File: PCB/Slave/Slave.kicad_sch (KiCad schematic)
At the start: 54 parts, among them J1 USB_C_Receptacle_USB2.0_16P, J2 Conn_01x05_Pin, J3 Conn_01x07_Socket, J4 Conn_01x04_Socket, J5 Conn_01x07_Socket, Q2 PNP, SW1 PTS810_SJM_250_SMTR_LFS, SW2 PTS810_SJM_250_SMTR_LFS, U1 ESP32-S3-MINI-1, U2 TCA9406DC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

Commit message: PCB-Update
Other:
- moved on the sheet: C1, C10, C12, C20, C9, J2, R11, U1

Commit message: Small changes to the pcb(Master and Slave))
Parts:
- C1: value u1F -> 100nF
- C19, C3, C4, C5, C7, C9: value 0u1F -> 100nF
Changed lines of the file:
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@@
 		(dnp no)
 		(property "Reference" "C5"
-			(at 86.9935 152.2437 90)
+			(at 92.964 153.416 90)
 			(effects
 				(font
@@
 			)
 		)
-		(property "Value" "0u1F"
-			(at 83.1835 152.2437 90)
+		(property "Value" "100nF"
+			(at 91.186 156.718 90)
 			(effects
 				(font
 					(size 1.27 1.27)
 				)
-				(hide yes)
 			)
 		)
@@
 			)
 		)
-		(property "Value" "u1F"
-			(at 325.12 45.212 0)
+		(property "Value" "100nF"
+			(at 323.088 45.212 0)
 			(effects
 				(font
@@
 			)
 		)
-		(property "Value" "0u1F"
+		(property "Value" "100nF"
 			(at 217.297 200.406 0)
 			(effects
@@
 			)
 		)
-		(property "Value" "0u1F"
+		(property "Value" "100nF"
 			(at 42.164 128.016 0)
 			(effects
@@
 			)
 		)
-		(property "Value" "0u1F"
+		(property "Value" "100nF"
 			(at 59.182 160.782 0)
 			(effects
@@
 			)
 		)
-		(property "Value" "0u1F"
+		(property "Value" "100nF"
 			(at 84.074 128.016 0)
 			(effects
@@
 		)
 		(property "Value" "GND"
-			(at 366.776 179.578 0)
+			(at 367.792 182.372 0)
 			(effects
 				(font
@@
 			)
 		)
-		(property "Value" "0u1F"
+		(property "Value" "100nF"
 			(at 364.744 178.816 0)
 			(effects

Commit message: Added CAP
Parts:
- added C21, C23: 100nF, Capacitor_SMD:C_0603_1608Metric_Pad1.08x0.95mm_HandSolder, symbol Device:C
- added C22: 1uF, Capacitor_SMD:C_0603_1608Metric_Pad1.08x0.95mm_HandSolder, symbol Device:C
- added C24: u1F, Capacitor_SMD:C_0603_1608Metric_Pad1.08x0.95mm_HandSolder, symbol Device:C
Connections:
- net ESP_3V3: now also C11.1, Q2.3 (E), U5.1 (VSUP), U5.16 (DVDD), C21.1, C22.1, C24.1
- net GND: now also C21.2, C22.2, C23.1, C24.2
- net VCC_5V: now also C23.2
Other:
- moved on the sheet: C1, C10, C11, C12, C13, C14, C15, C16, C17, C18, C19, C20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

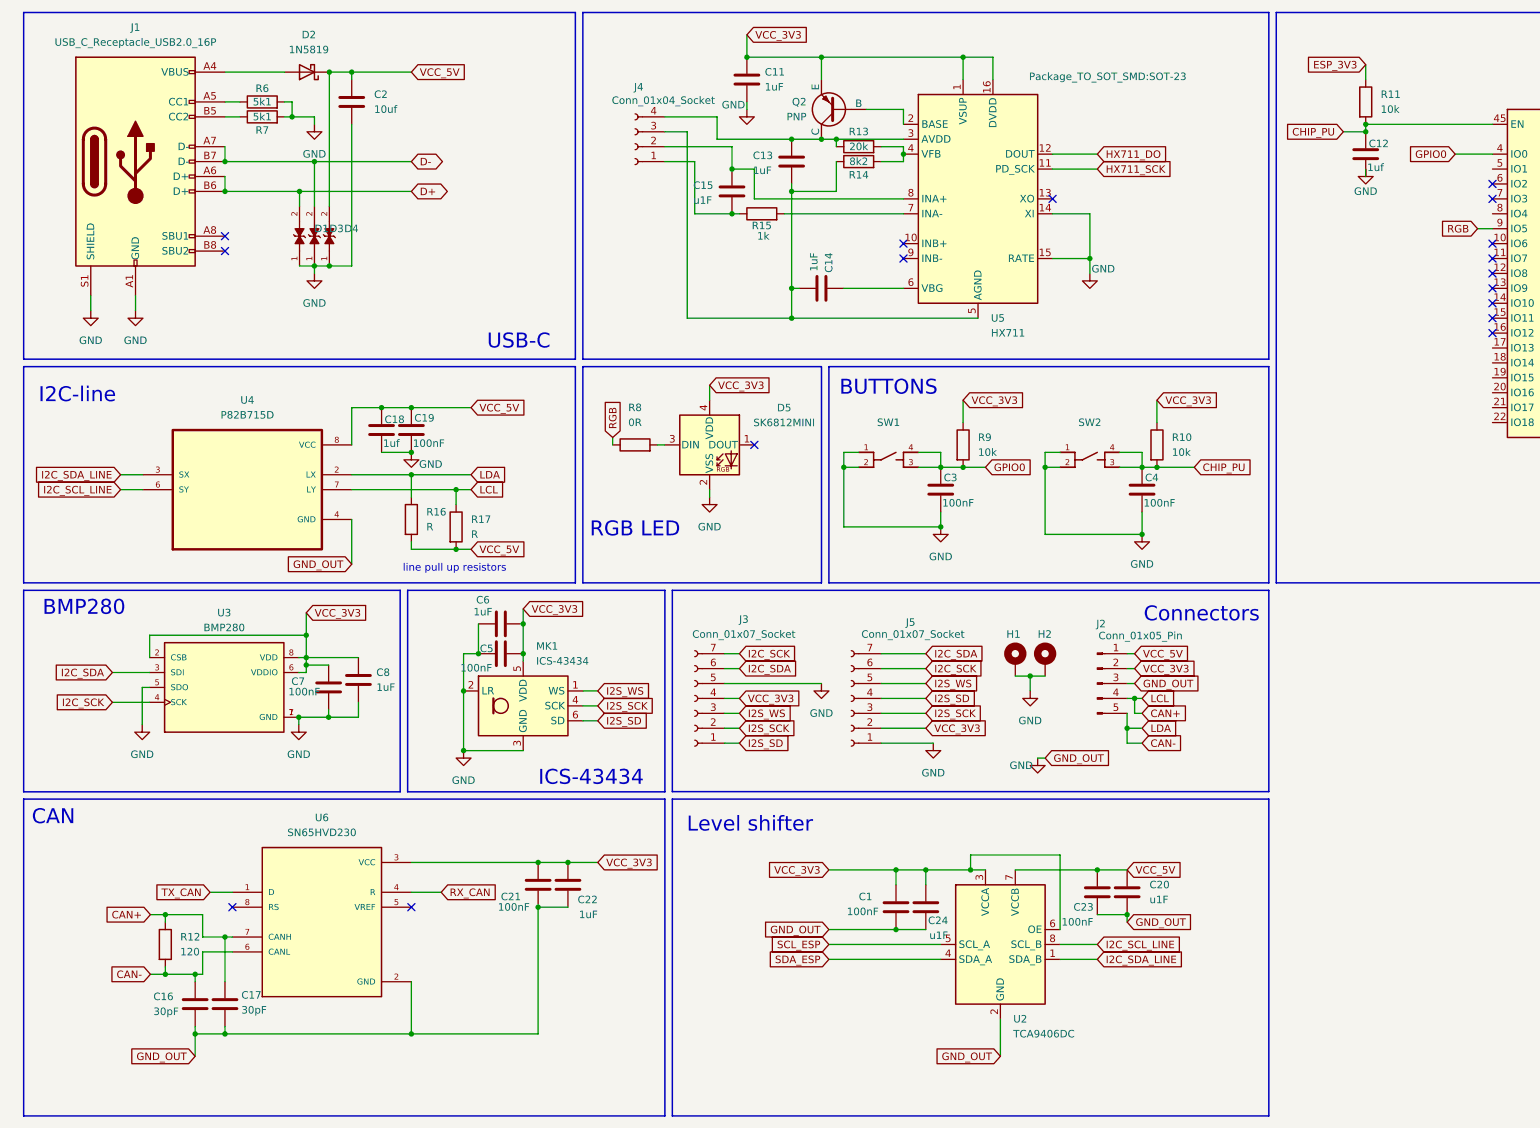
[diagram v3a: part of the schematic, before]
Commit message: Changed bmp for bme
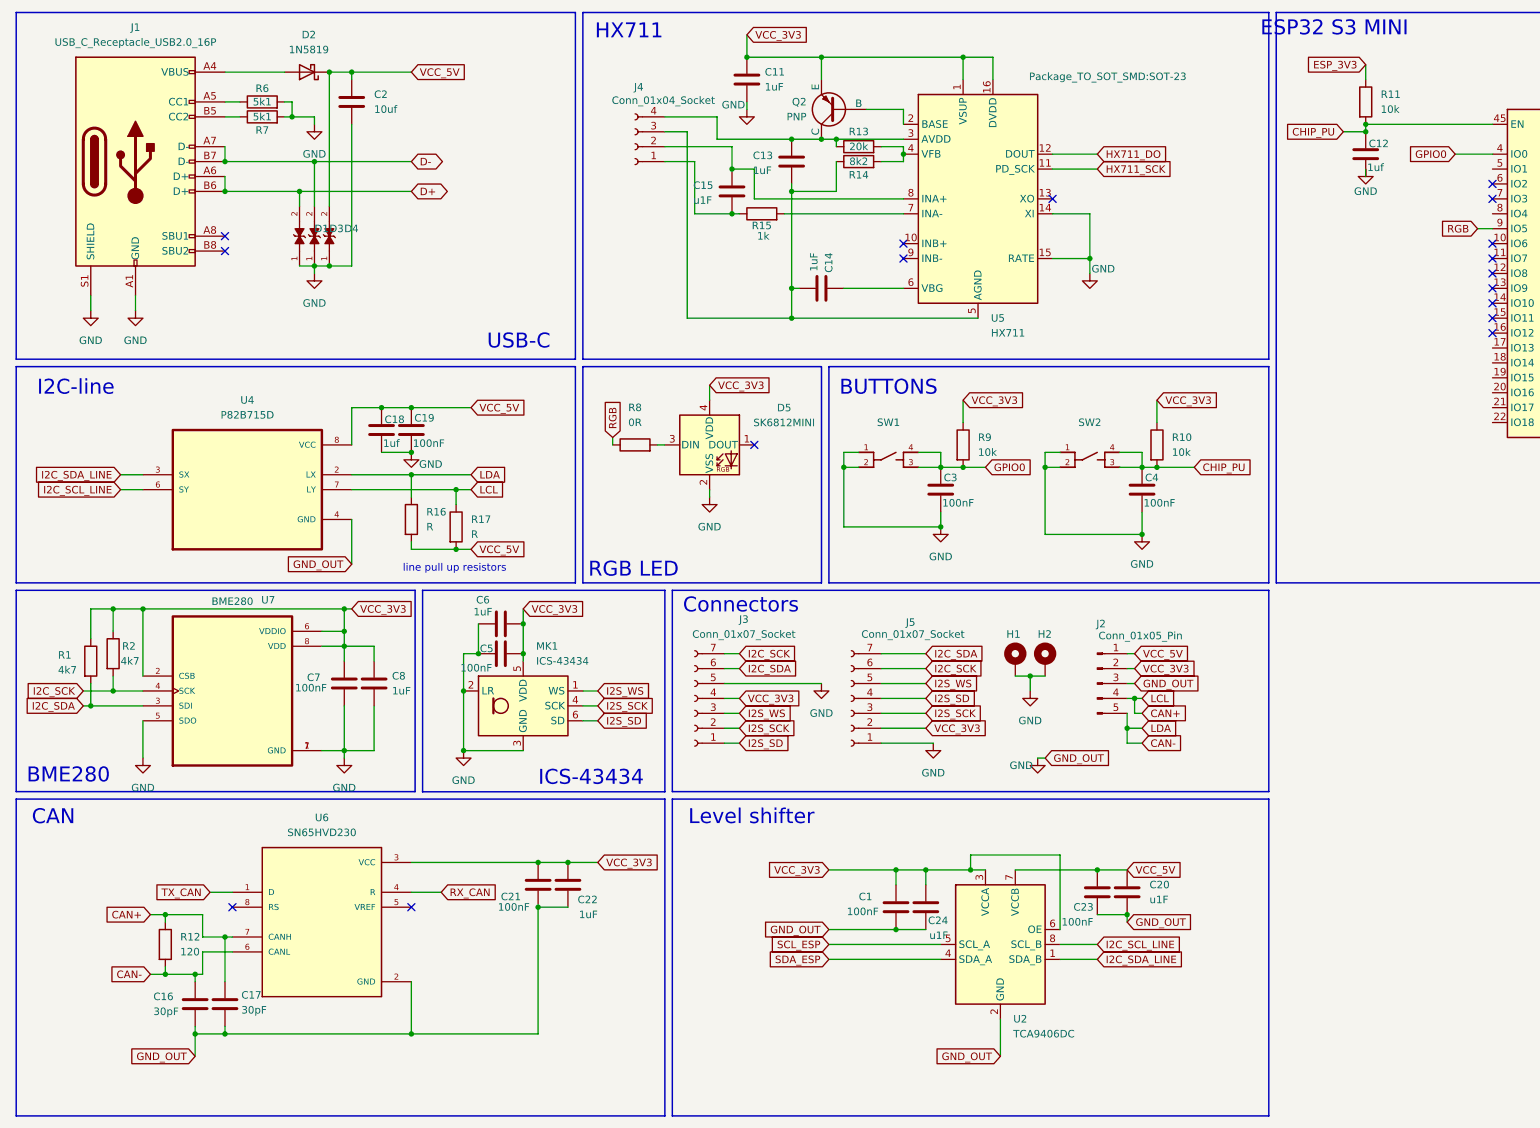
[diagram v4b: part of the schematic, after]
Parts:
- removed U3: BMP280, BMP280:XDCR_BMP280, symbol BMP280:BMP280
- added R1, R2: 4k7, Resistor_SMD:R_0603_1608Metric_Pad0.98x0.95mm_HandSolder, symbol Device:R
- added U7: BME280, BME280:PSON65P250X250X100-8N, symbol BME280:BME280
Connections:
- net ESP_3V3: now also R1.1, R2.1, U7.2 (CSB), U7.6 (VDDIO), U7.8 (VDD)
- net GND: now also U7.1 (GND), U7.5 (SDO), U7.7 (GND)
- net I2C_SCK: now also R2.2, U7.4 (SCK)
- net I2C_SDA: now also R1.2, U7.3 (SDI)
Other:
- note added: "BME280"
- note added: "ESP32 S3 MINI"
- note added: "HX711"
- note removed: "BMP280"
- moved on the sheet: C7, C8

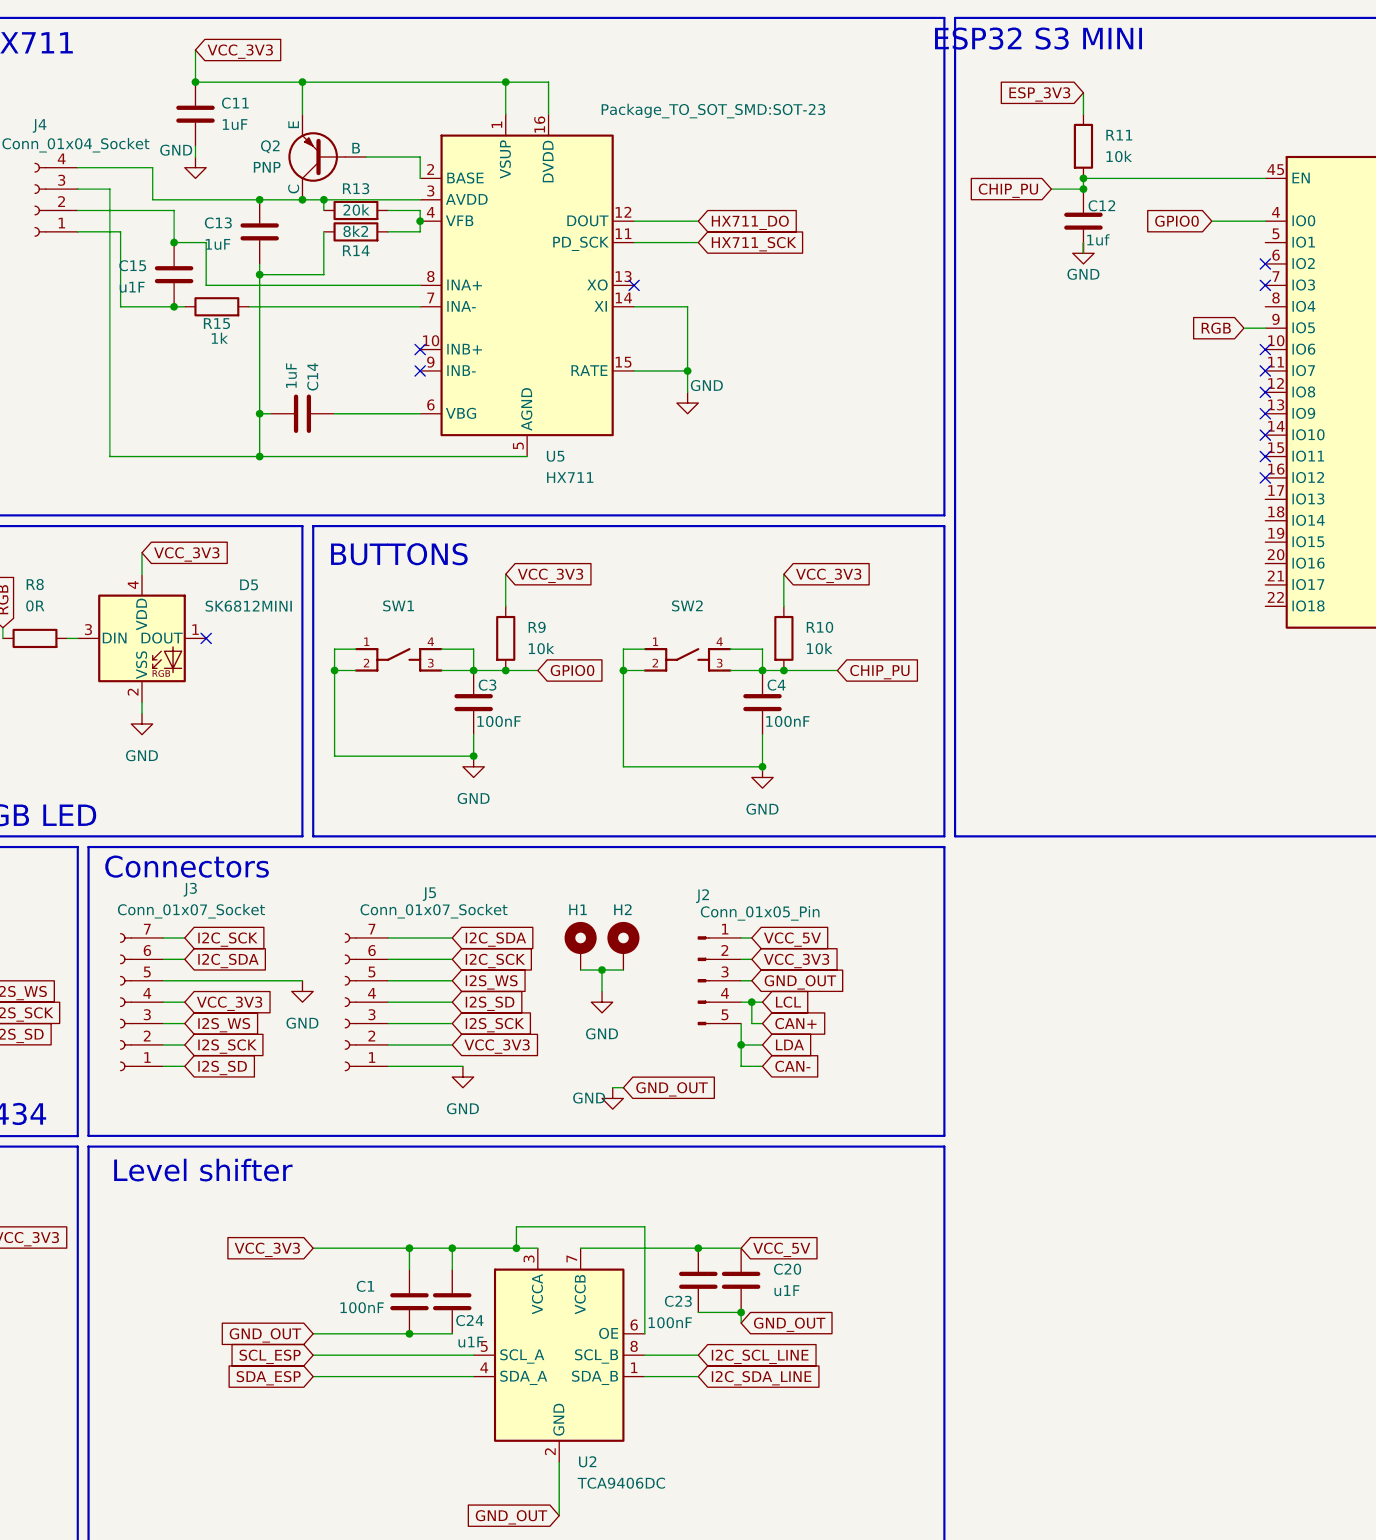
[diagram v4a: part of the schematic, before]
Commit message: Added I2C PullUp Resistors
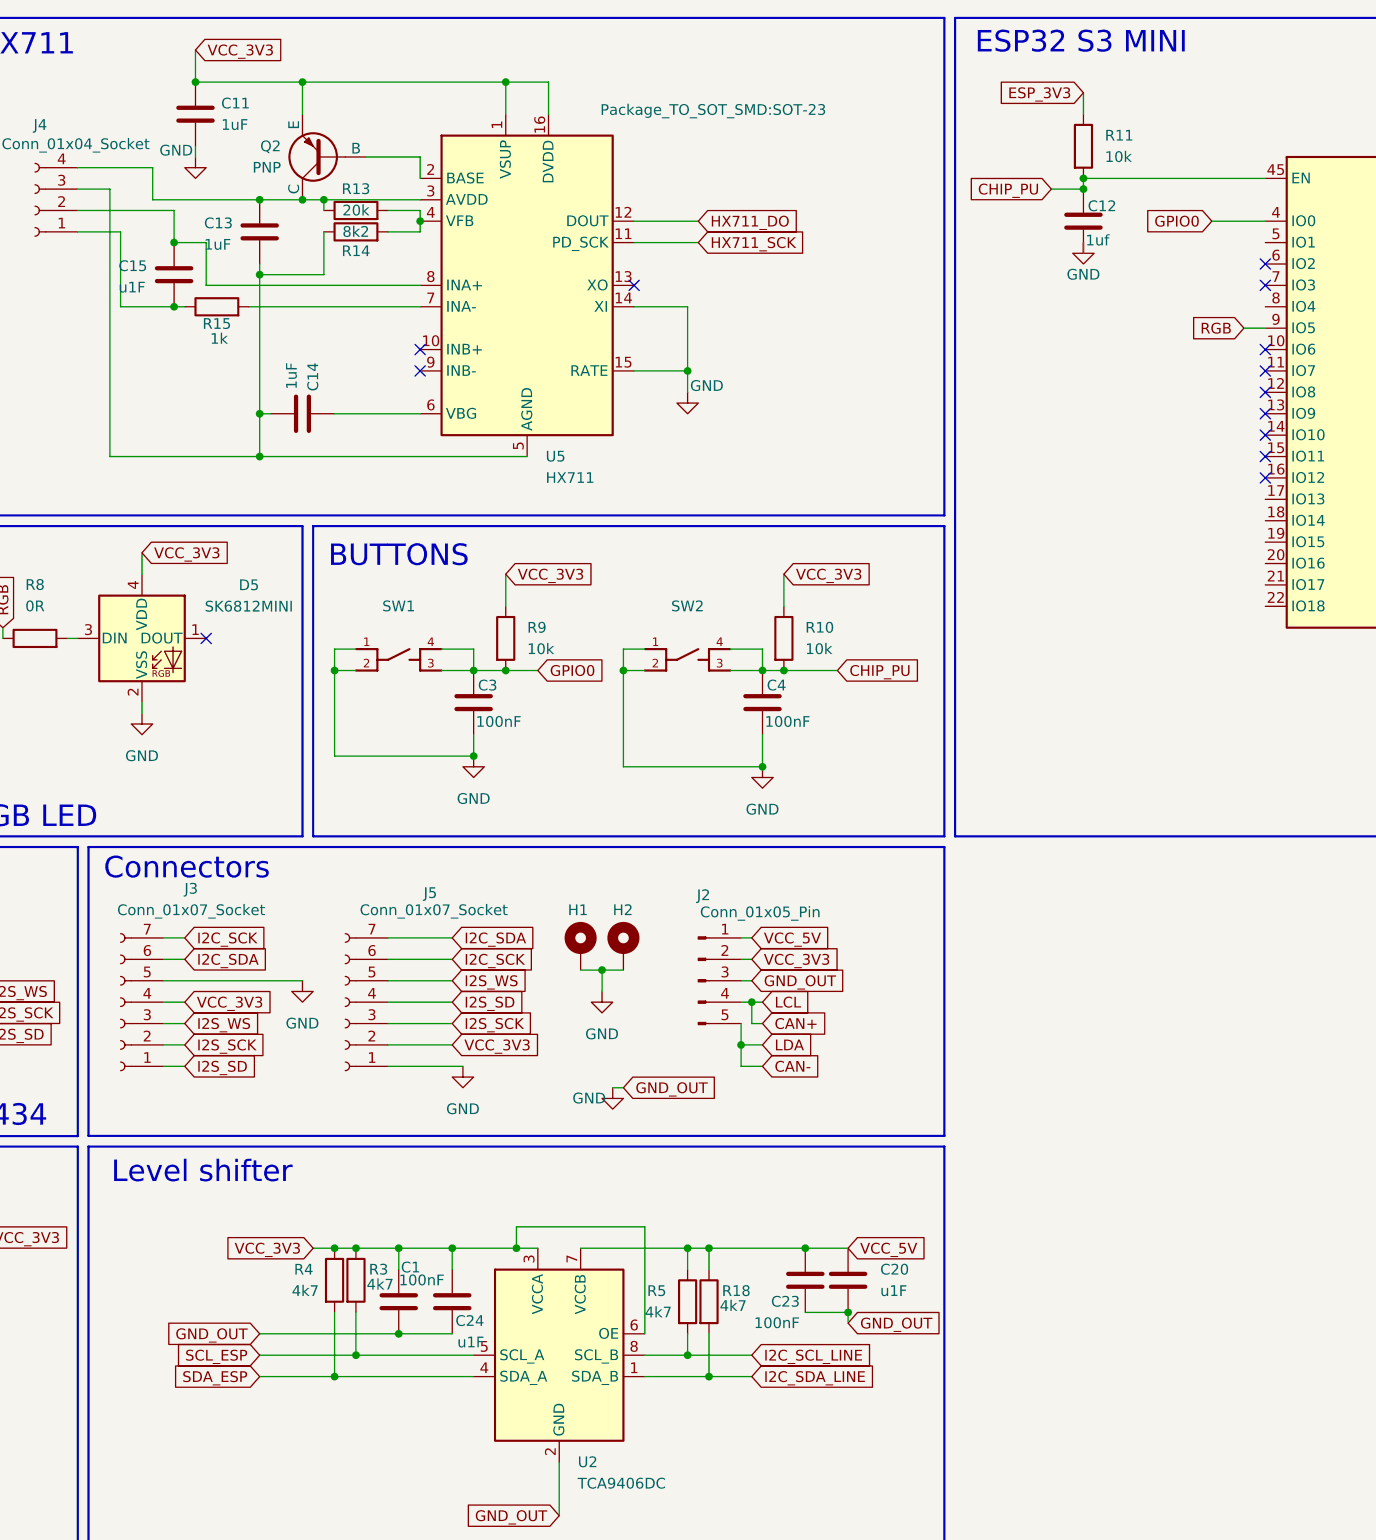
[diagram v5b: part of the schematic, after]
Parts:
- added R18, R3, R4, R5: 4k7, Resistor_SMD:R_0603_1608Metric_Pad0.98x0.95mm_HandSolder, symbol Device:R
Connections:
- net ESP_3V3: now also R3.1, R4.1
- net I2C_SCL_LINE: now also R5.2
- net I2C_SDA_LINE: now also R18.2
- net SCL_ESP: now also R3.2
- net SDA_ESP: now also R4.2
- net VCC_5V: now also R18.1, R5.1
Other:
- moved on the sheet: C1, C20, C23
